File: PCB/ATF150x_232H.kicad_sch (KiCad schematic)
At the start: 18 parts, among them J1 CJMCU-232H, J2 Altera JTAG-A+VPP, U1 ATF150x-xJx44 (PLCC-44), U2 MAX662A

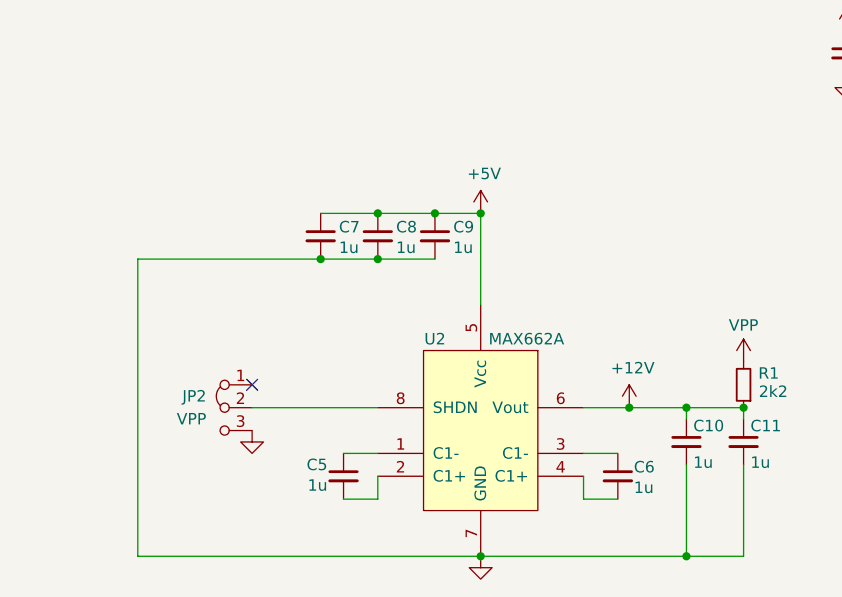
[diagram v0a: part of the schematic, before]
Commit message: switch power to max662 instead of using shutdown pin so vpp actually shuts off
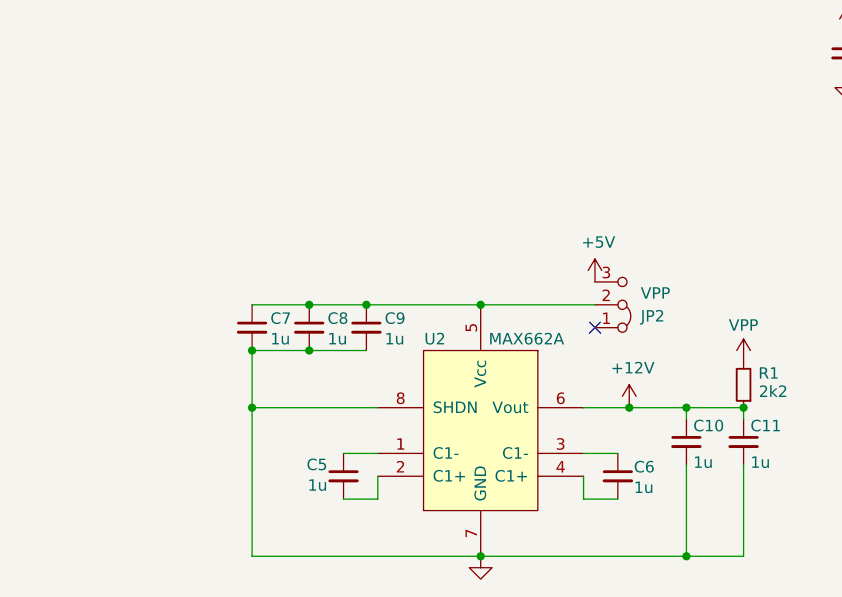
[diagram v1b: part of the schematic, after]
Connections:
- net +5V: now also JP2.3; no longer C7.1, C8.1, C9.1, U2.5 (Vcc)
- net GND: now also U2.8 (SHDN); no longer JP2.3
- net at JP2.2: now also C7.1, C8.1, C9.1, U2.5 (Vcc); no longer U2.8 (SHDN)
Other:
- moved on the sheet: C7, C8, C9, JP2
